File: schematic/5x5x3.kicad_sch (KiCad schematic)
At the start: 111 parts, among them J1 SW Debug, SW11 SW, SW12 SW, SW13 SW, SW14 SW, SW15 SW, SW21 SW, SW22 SW, SW23 SW, SW24 SW, SW25 SW, SW31 SW, SW32 SW, SW33 SW, SW34 SW, SW35 SW, SW41 SW, SW42 SW, SW43 SW, SW44 SW, SW45 SW, SW51 SW, SW52 SW, SW53 SW, SW54 SW, SW55 SW, SW6 ALPS_EC11, U1 nice_nano

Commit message: Started with layout
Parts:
- LED11: value SK6812MINI-E -> SK68XXMINI-E
- SW11, SW12, SW13, SW14, SW21, SW22, SW23, SW24, SW25, SW31, SW32, SW33, SW34, SW35, SW41, SW42, SW43, SW44, SW45, SW51, SW52, SW53, SW54, SW55: footprint keyswitch:SW_Hotswap_Kailh_MX_1.00u -> footprints:SW_Hotswap_Kailh_Choc_V1V2_1.00u
- SW15: footprint keyswitch:SW_Hotswap_Kailh_MX_1.00u -> PCM_Switch_Keyboard_Hotswap_Kailh:SW_Hotswap_Kailh_Choc_V1V2_1.00u; now not fitted
- U1: value nice_nano -> nice_nano v2; footprint PCM_marbastlib-xp-promicroish:nice_nano_AH_USBup -> footprints:nice_nano_AH_USBup
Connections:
- net BACKLIGHTIN: now also U1.5 (P0.17)
- net COL1: now also U1.17 (P0.31-LF)
- net COL2: now also U1.18 (P0.29-LF)
- net COL3: now also U1.19 (P0.02-LF)
- net COL4: now also U1.20 (P1.15-LF)
- net COL5: now also U1.21 (P1.13-LF)
- net ROTA: now also U1.25 (P1.01-LF)
- net ROTB: now also U1.26 (P1.02-LF)
- net ROTD: now also U1.22 (P1.11-LF)
- net ROW2: now also U1.23 (P0.10-LF)
- net ROW3: now also U1.24 (P0.09-LF)
- net ROW4: now also U1.8 (P0.24)
- net ROW5: now also U1.9 (P1.00)
- net SWDIO: now reaches J1.2 (Pin_2)
- net SWDIO: now also U1.J3 (SWDIO)
- net SWCLK: now reaches J1.3 (Pin_3)
- net SWCLK: now also U1.J4 (SWCLK)
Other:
- moved on the sheet: C11, C12, C13, C14, C15, C19, C20, C21, C22, C23, C24, C25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

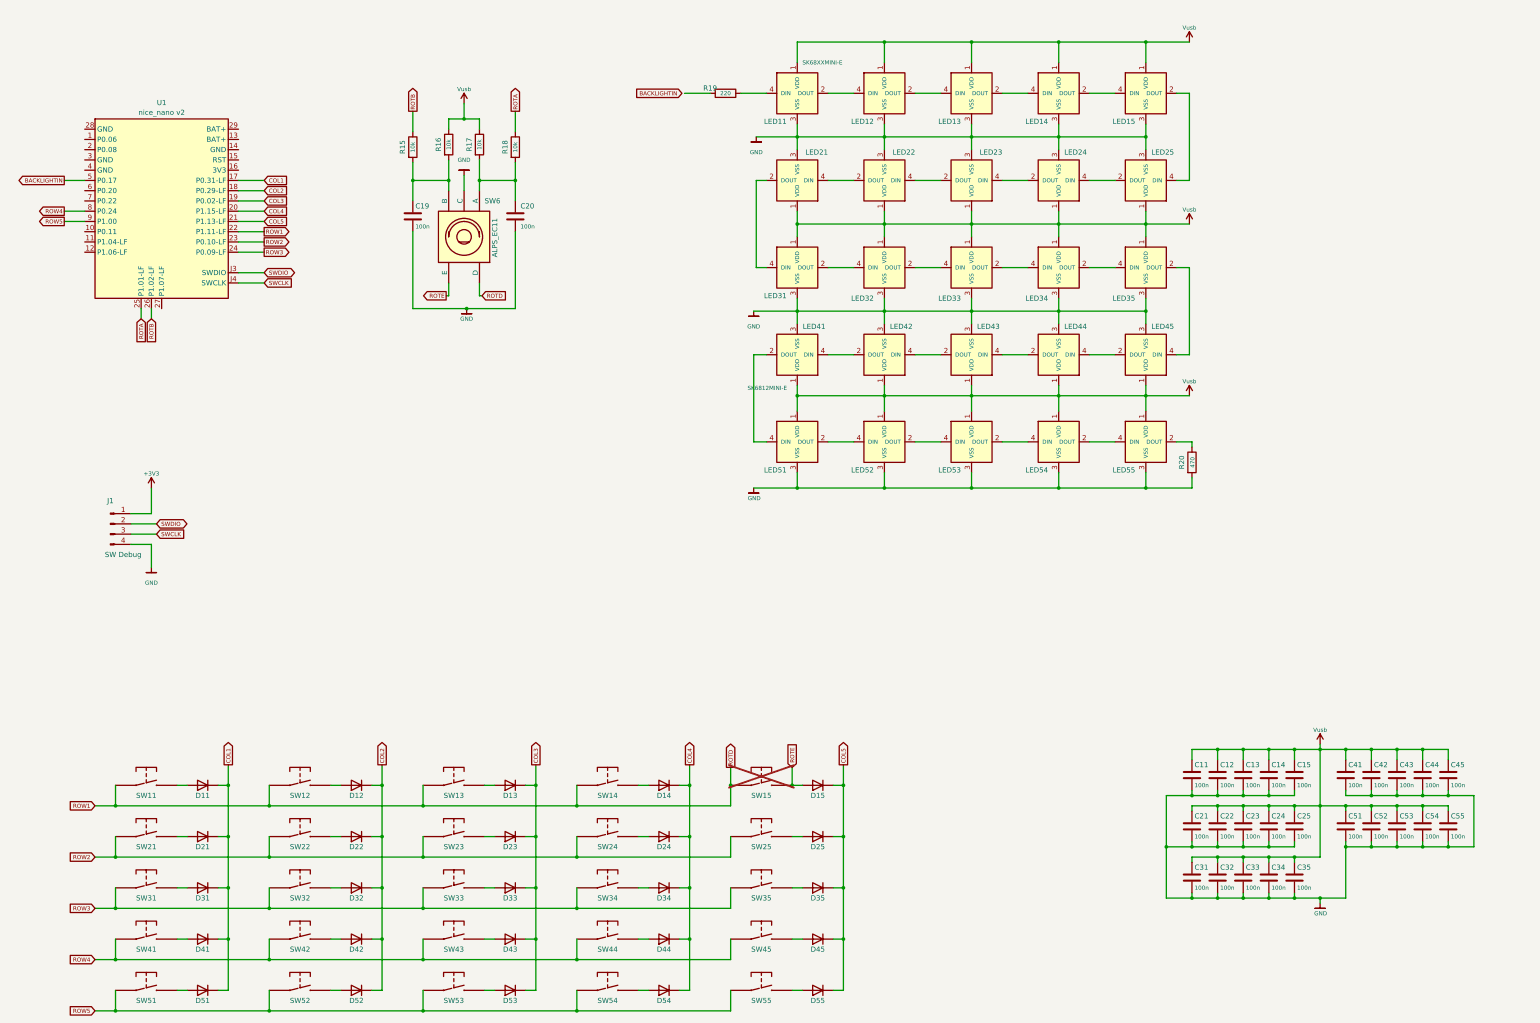
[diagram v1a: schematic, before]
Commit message: Connect up the keys, rough placing of components
Need to find a good switch, and maybe rearrange the row / col pins to
better align with 5x5 layout.

Currently targetting 4 layer board
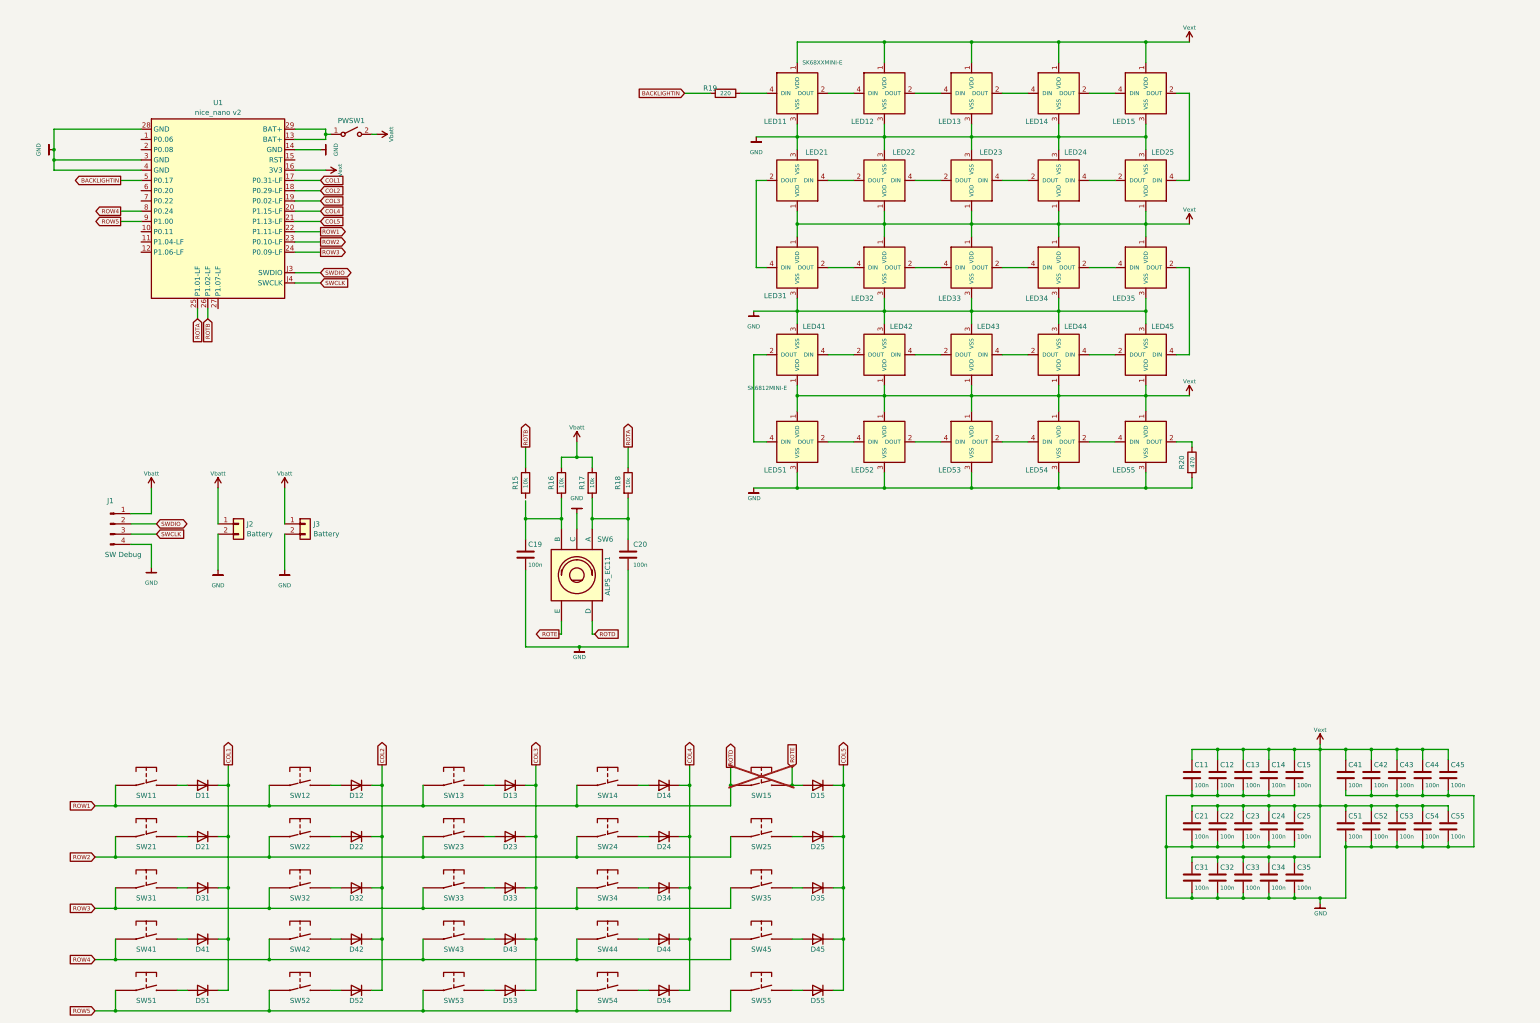
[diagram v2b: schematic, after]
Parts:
- added J2, J3: Battery, Connector_JST:JST_GH_BM02B-GHS-TBT_1x02-1MP_P1.25mm_Vertical, symbol Connector_Generic:Conn_01x02
- added PWSW1: SW_SPST, Button_Switch_THT:SW_E-Switch_EG1224_SPDT_Angled, symbol Switch:SW_SPST
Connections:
- net BACKLIGHTIN: now also R19.2
- net GND: now also U1.14 (GND), U1.28 (GND), U1.3 (GND), U1.4 (GND), J2.2 (Pin_2), J3.2 (Pin_2)
- net at C19.1, R16.2, SW6.B: no longer R15.2
- net at U1.13 (BAT+): now also U1.29 (BAT+), PWSW1.1 (A)
- net Vext: now reaches U1.16 (3V3)
- net Vext: now also C11.1, C12.1, C13.1, C14.1, C15.1, C21.1, C22.1, C23.1, C24.1, C25.1, C31.1, C32.1, C33.1, C34.1, C35.1, C41.1, C42.1, C43.1, C44.1, C45.1, C51.1, C52.1, C53.1, C54.1, C55.1, LED11.1 (VDD), LED12.1 (VDD), LED13.1 (VDD), LED14.1 (VDD), LED15.1 (VDD), LED21.1 (VDD), LED22.1 (VDD), LED23.1 (VDD), LED24.1 (VDD), LED25.1 (VDD), LED31.1 (VDD), LED32.1 (VDD), LED33.1 (VDD), LED34.1 (VDD), LED35.1 (VDD), LED41.1 (VDD), LED42.1 (VDD), LED43.1 (VDD), LED44.1 (VDD), LED45.1 (VDD), LED51.1 (VDD), LED52.1 (VDD), LED53.1 (VDD), LED54.1 (VDD), LED55.1 (VDD)
- net +3V3 renamed Vbatt
- net Vbatt: now also R16.1, R17.1, J2.1 (Pin_1), J3.1 (Pin_1), PWSW1.2 (B)
- removed net Vusb: C11.1, C12.1, C13.1, C14.1, C15.1, C21.1, C22.1, C23.1, C24.1, C25.1, C31.1, C32.1, C33.1, C34.1, C35.1, C41.1, C42.1, C43.1, C44.1, C45.1, C51.1, C52.1, C53.1, C54.1, C55.1, LED11.1 (VDD), LED12.1 (VDD), LED13.1 (VDD), LED14.1 (VDD), LED15.1 (VDD), LED21.1 (VDD), LED22.1 (VDD), LED23.1 (VDD), LED24.1 (VDD), LED25.1 (VDD), LED31.1 (VDD), LED32.1 (VDD), LED33.1 (VDD), LED34.1 (VDD), LED35.1 (VDD), LED41.1 (VDD), LED42.1 (VDD), LED43.1 (VDD), LED44.1 (VDD), LED45.1 (VDD), LED51.1 (VDD), LED52.1 (VDD), LED53.1 (VDD), LED54.1 (VDD), LED55.1 (VDD), R16.1, R17.1
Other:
- moved on the sheet: C19, C20, R15, R16, R17, R18, SW6, U1

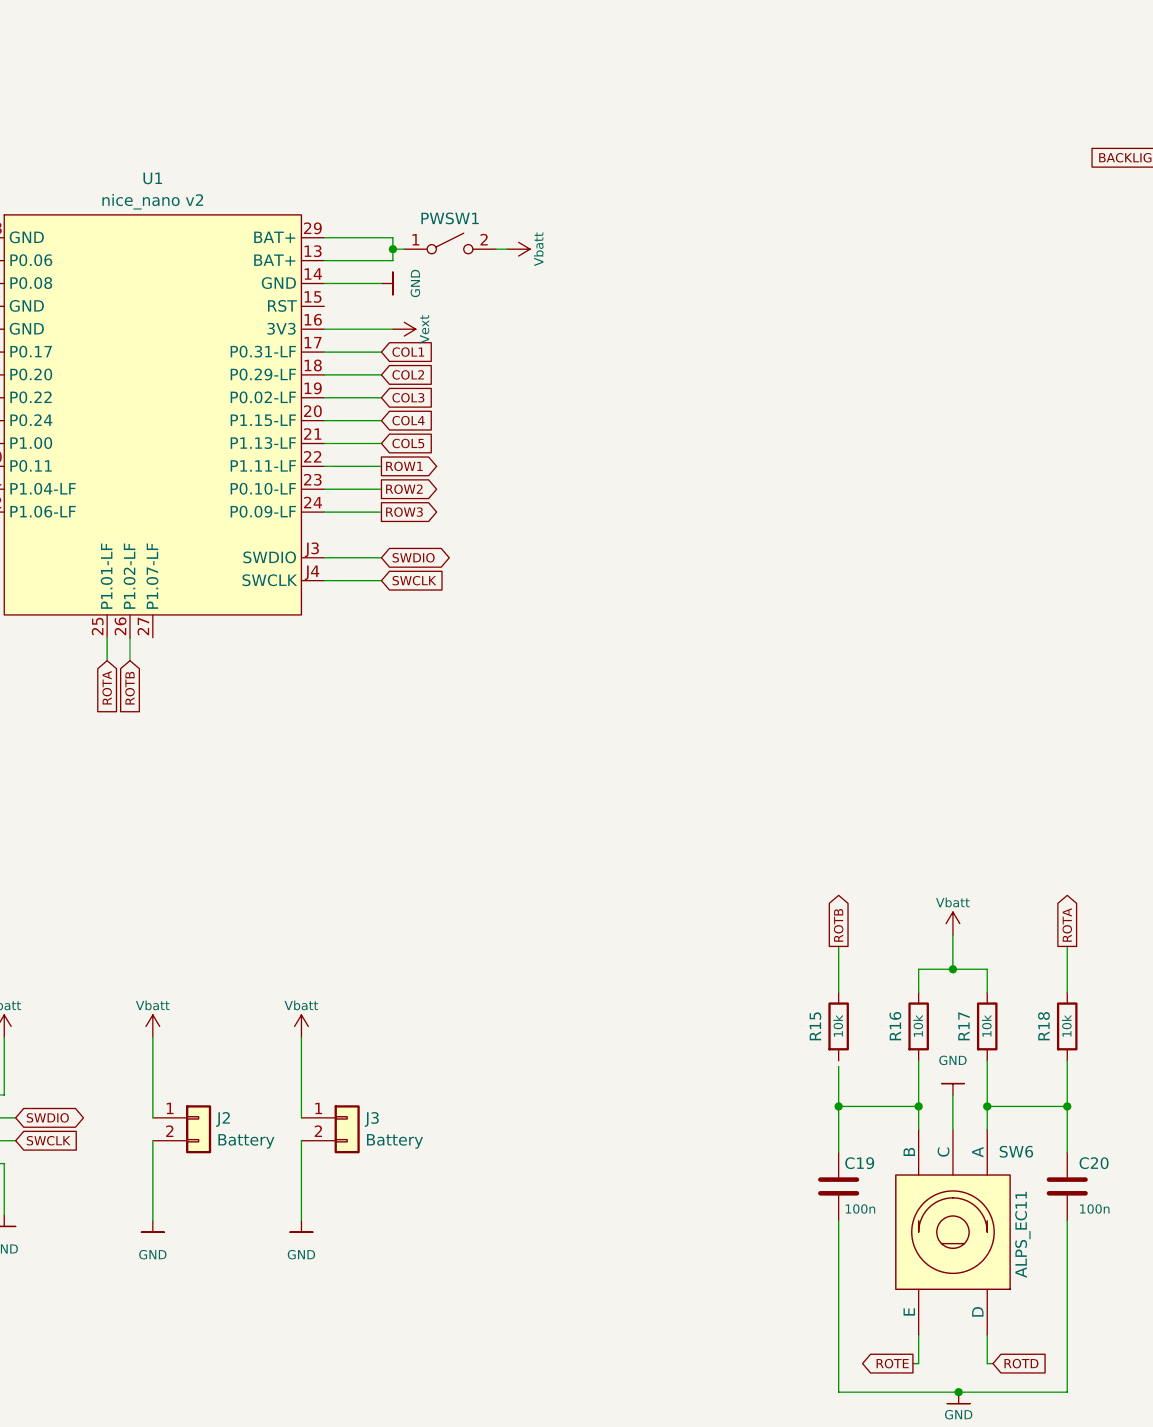
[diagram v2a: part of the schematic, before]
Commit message: Adjusted powerswitch, battery terminal, rotary encoder
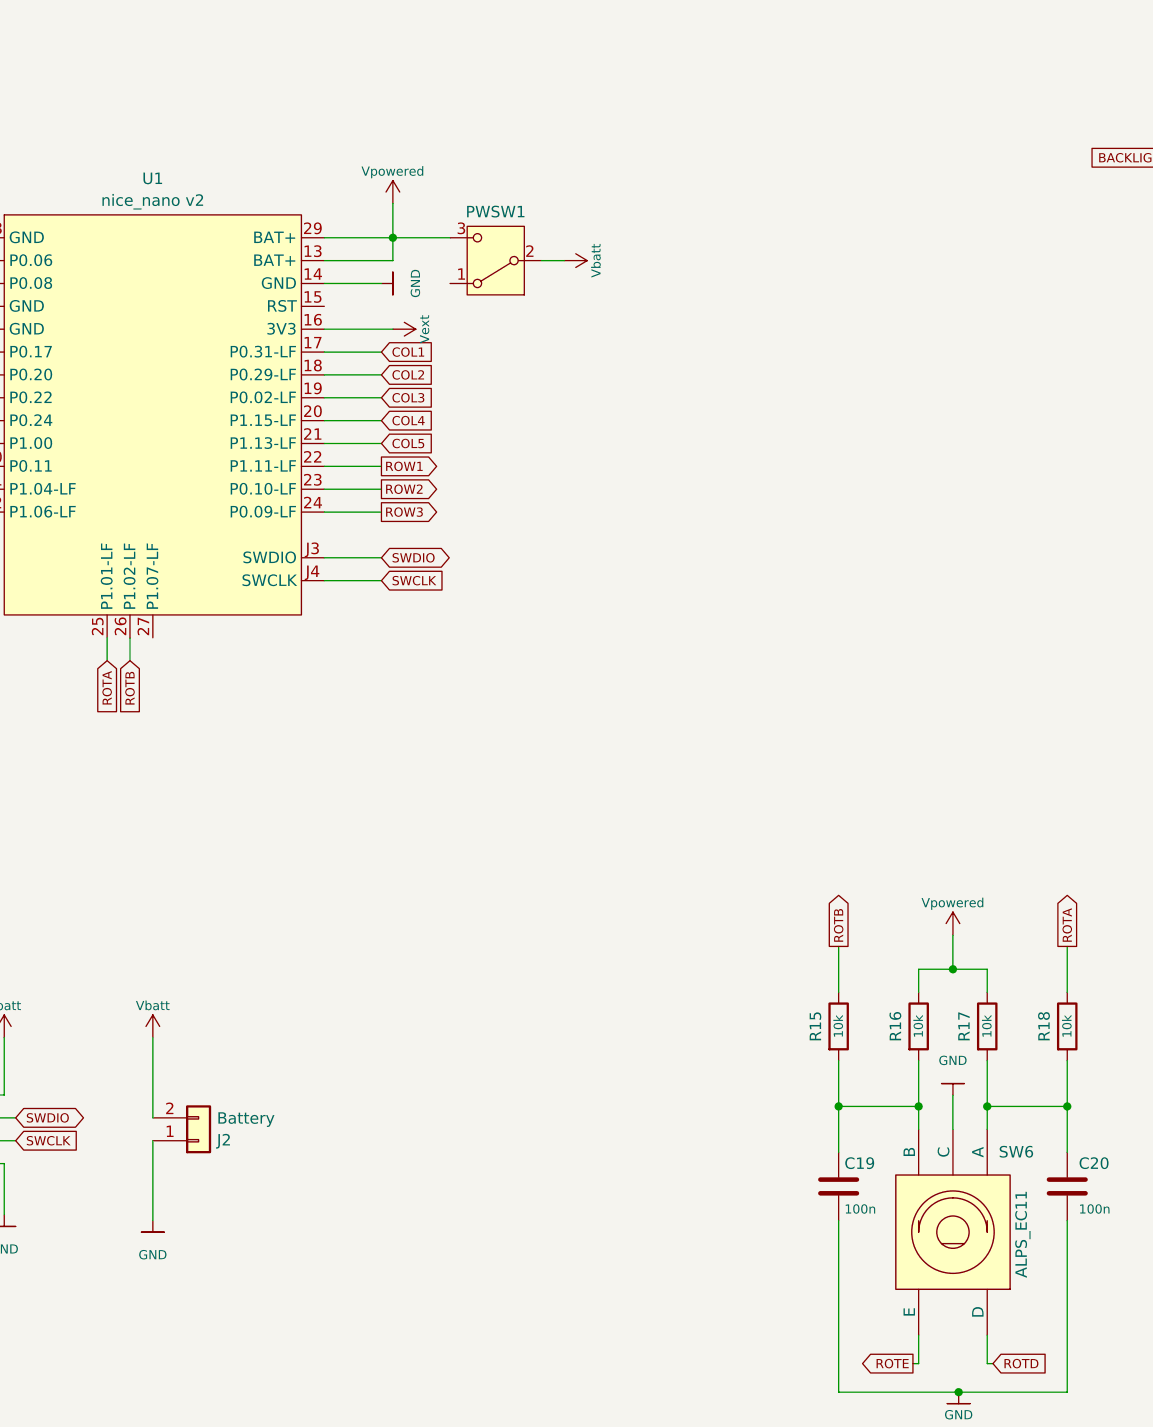
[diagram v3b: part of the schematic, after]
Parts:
- removed J3: Battery, Connector_JST:JST_GH_BM02B-GHS-TBT_1x02-1MP_P1.25mm_Vertical, symbol Connector_Generic:Conn_01x02
- PWSW1: footprint Button_Switch_THT:SW_E-Switch_EG1224_SPDT_Angled -> PCM_marbastlib-various:SW_MSK12C02-HB; symbol Switch:SW_SPST -> Switch:SW_SPDT
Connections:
- net GND: now also J2.1 (Pin_1); no longer J2.2 (Pin_2)
- net Vbatt: now also J2.2 (Pin_2); no longer J2.1 (Pin_1), R16.1, R17.1
- net at C19.1, R16.2, SW6.B: now also R15.2
- net Vpowered: now reaches U1.13 (BAT+), U1.29 (BAT+)
- net Vpowered: now also PWSW1.3 (C), R16.1, R17.1; no longer PWSW1.1 (A)
